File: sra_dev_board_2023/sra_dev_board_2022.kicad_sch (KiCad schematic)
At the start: 74 parts, among them J1 Conn_01x19_Male, J10 Conn_01x03_Male, J11 Conn_01x05_Male, J12 Conn_01x05_Male, J13 Conn_01x05_Male, J14 Conn_01x03_Male, J15 Conn_01x03_Male, J16 Screw_Terminal_01x05, J2 Conn_01x03_Male, J3 Conn_01x03_Male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

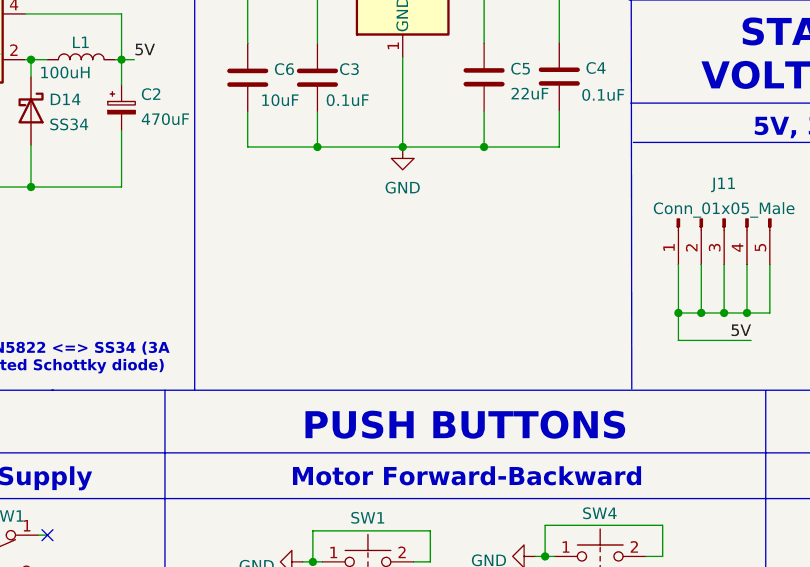
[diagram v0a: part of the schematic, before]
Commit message: Updated gerbers for LSA and SRA-Board
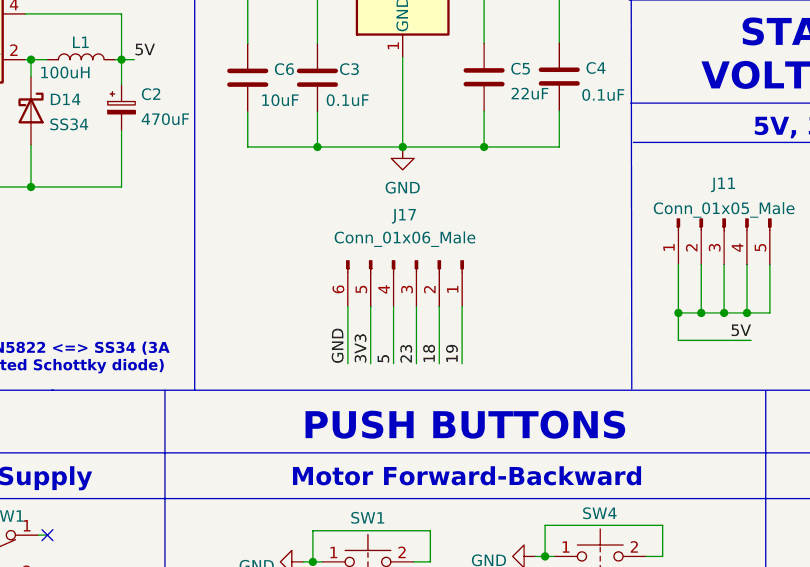
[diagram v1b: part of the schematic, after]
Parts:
- added J17: Conn_01x06_Male, Connector_PinHeader_2.54mm:PinHeader_1x06_P2.54mm_Vertical, symbol Connector:Conn_01x06_Male
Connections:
- net 18: now also J17.2 (Pin_2)
- net 19: now also J17.1 (Pin_1)
- net 23: now also J17.3 (Pin_3)
- net 3V3: now also J17.5 (Pin_5)
- net 5: now also J17.4 (Pin_4)
- net GND: now also J17.6 (Pin_6)
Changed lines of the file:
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@@
     (stroke (width 0) (type default) (color 0 0 0 0))
   )
+  (wire (pts (xy 198.12 78.74) (xy 198.12 85.09))
+    (stroke (width 0) (type default) (color 0 0 0 0))
+  )
   (wire (pts (xy 72.5678 178.8668) (xy 72.5678 182.6768))
     (stroke (width 0) (type default) (color 0 0 0 0))
@@
     (stroke (width 0) (type default) (color 0 0 0 0))
   )
+  (wire (pts (xy 203.2 78.74) (xy 203.2 85.09))
+    (stroke (width 0) (type default) (color 0 0 0 0))
+  )
   (wire (pts (xy 180.34 181.61) (xy 182.88 181.61))
     (stroke (width 0) (type default) (color 0 0 0 0))
@@
     (stroke (width 0) (type default) (color 0 0 0 0))
   )
+  (wire (pts (xy 205.74 78.74) (xy 205.74 85.09))
+    (stroke (width 0) (type default) (color 0 0 0 0))
+  )
   (wire (pts (xy 72.1614 45.466) (xy 82.169 45.466))
     (stroke (width 0) (type default) (color 0 0 0 0))
@@
     (stroke (width 0) (type default) (color 0 0 0 0))
   )
+  (wire (pts (xy 208.28 78.74) (xy 208.28 85.09))
+    (stroke (width 0) (type default) (color 0 0 0 0))
+  )
   (wire (pts (xy 242.57 186.69) (xy 245.11 186.69))
     (stroke (width 0) (type default) (color 0 0 0 0))
@@
     (stroke (width 0) (type default) (color 0 0 0 0))
   )
+  (wire (pts (xy 200.66 78.74) (xy 200.66 85.09))
+    (stroke (width 0) (type default) (color 0 0 0 0))
+  )
   (wire (pts (xy 253.1872 82.4738) (xy 261.2644 82.4738))
     (stroke (width 0) (type default) (color 0 0 0 0))
@@
     (stroke (width 0) (type default) (color 0 0 0 0))
   )
+  (wire (pts (xy 210.82 78.74) (xy 210.82 85.09))
+    (stroke (width 0) (type default) (color 0 0 0 0))
+  )
   (polyline (pts (xy 59.182 135.2804) (xy 59.3598 135.2804))
     (stroke (width 0) (type default) (color 0 0 0 0))
@@
     (effects (font (size 1.27 1.27)) (justify left bottom))
   )
+  (label "18" (at 208.28 85.09 90)
+    (effects (font (size 1.27 1.27)) (justify left bottom))
+  )
   (label "3V3" (at 283.21 168.91 180)
     (effects (font (size 1.27 1.27)) (justify right bottom))
@@
     (effects (font (size 1.27 1.27)) (justify right bottom))
   )
+  (label "23" (at 205.74 85.09 90)
+    (effects (font (size 1.27 1.27)) (justify left bottom))
+  )
   (label "AIN2" (at 265.43 201.0664 180)
     (effects (font (size 1.27 1.27)) (justify right bottom))
@@
     (effects (font (size 1.27 1.27)) (justify left bottom))
   )
+  (label "GND" (at 198.12 85.09 90)
+    (effects (font (size 1.27 1.27)) (justify left bottom))
+  )
   (label "35" (at 128.27 163.83 180)
     (effects (font (size 1.27 1.27)) (justify right bottom))
@@
     (effects (font (size 1.27 1.27)) (justify left bottom))
   )
+  (label "5" (at 203.2 85.09 90)
+    (effects (font (size 1.27 1.27)) (justify left bottom))
+  )
   (label "AIN1" (at 260.35 201.0664 180)
     (effects (font (size 1.27 1.27)) (justify right bottom))
@@
     (effects (font (size 1.27 1.27)) (justify right bottom))
   )
+  (label "3V3" (at 200.66 85.09 90)
+    (effects (font (size 1.27 1.27)) (justify left bottom))
+  )
   (label "M0" (at 180.34 179.07 0)
     (effects (font (size 1.27 1.27)) (justify left bottom))
@@
     (effects (font (size 1.27 1.27)) (justify left bottom))
   )
+  (label "19" (at 210.82 85.09 90)
+    (effects (font (size 1.27 1.27)) (justify left bottom))
+  )
   (label "5" (at 27.8638 220.3958 180)
     (effects (font (size 1.27 1.27)) (justify right bottom))
@@
     (pin "9")
   )
+  (symbol (lib_id "Connector:Conn_01x06_Male") (at 205.74 73.66 270) (unit 1)
+    (in_bom yes) (on_board yes) (fields_autoplaced)
+    (property "Reference" "J17" (id 0) (at 204.47 68.58 90))
+    (property "Value" "Conn_01x06_Male" (id 1) (at 204.47 71.12 90))
+    (property "Footprint" "Connector_PinHeader_2.54mm:PinHeader_1x06_P2.54mm_Vertical" (id 2) (at 205.74 73.66 0)
+      (effects (font (size 1.27 1.27)) hide)
+    )
+    (property "Datasheet" "~" (id 3) (at 205.74 73.66 0)
+      (effects (font (size 1.27 1.27)) hide)
+    )
+    (pin "1")
+    (pin "2")
+    (pin "3")
+    (pin "4")
+    (pin "5")
+    (pin "6")
+  )
   (symbol (lib_id "Switch:SW_Push_DPDT") (at 98.9584 111.76 0) (unit 1)
     (in_bom yes) (on_board yes)
@@
       (reference "J16") (unit 1) (value "Screw_Terminal_01x05") (footprint "TerminalBlock:TerminalBlock_bornier-5_P5.08mm")
     )
+    (path "/618ea879-4cfc-4447-a45c-89b029d0fa10"
+      (reference "J17") (unit 1) (value "Conn_01x06_Male") (footprint "Connector_PinHeader_2.54mm:PinHeader_1x06_P2.54mm_Vertical")
+    )
     (path "/f7739dc8-da06-4162-a76b-6df1c594100c"
